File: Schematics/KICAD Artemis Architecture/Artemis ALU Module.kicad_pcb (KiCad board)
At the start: 4 copper layers, 66.2 x 46 mm, 11 parts, among them J1 B Input Socket, J2 A Input Socket, J3 F Output Socket, J4 Control Word Socket, J5 Flag Socket, J6 Power Socket, U1 74LS181, U2 74LS181, U3 74LS30

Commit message: Register PCB Created and Finished
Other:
- board text added: "ALU V1"
- board text removed: "ALU Module"

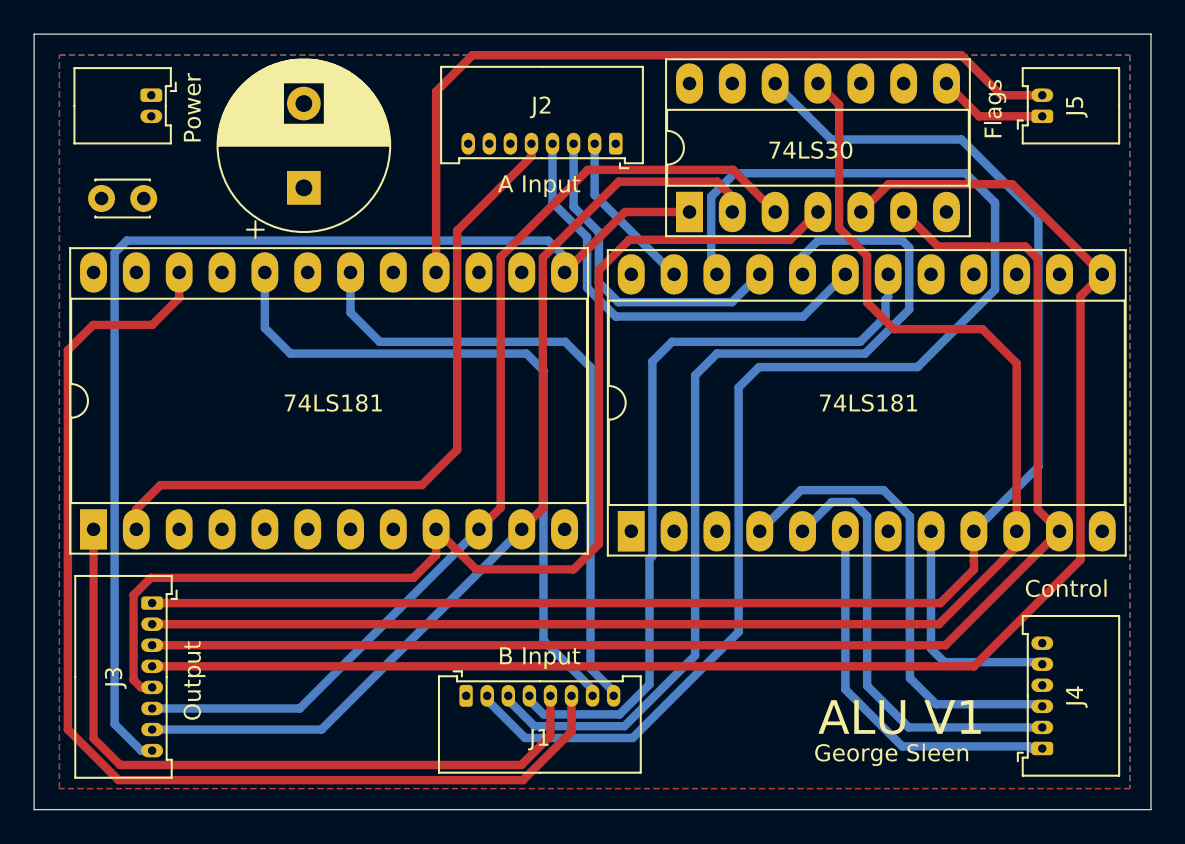
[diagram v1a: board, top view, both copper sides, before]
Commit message: Cleaned up ALU PCB
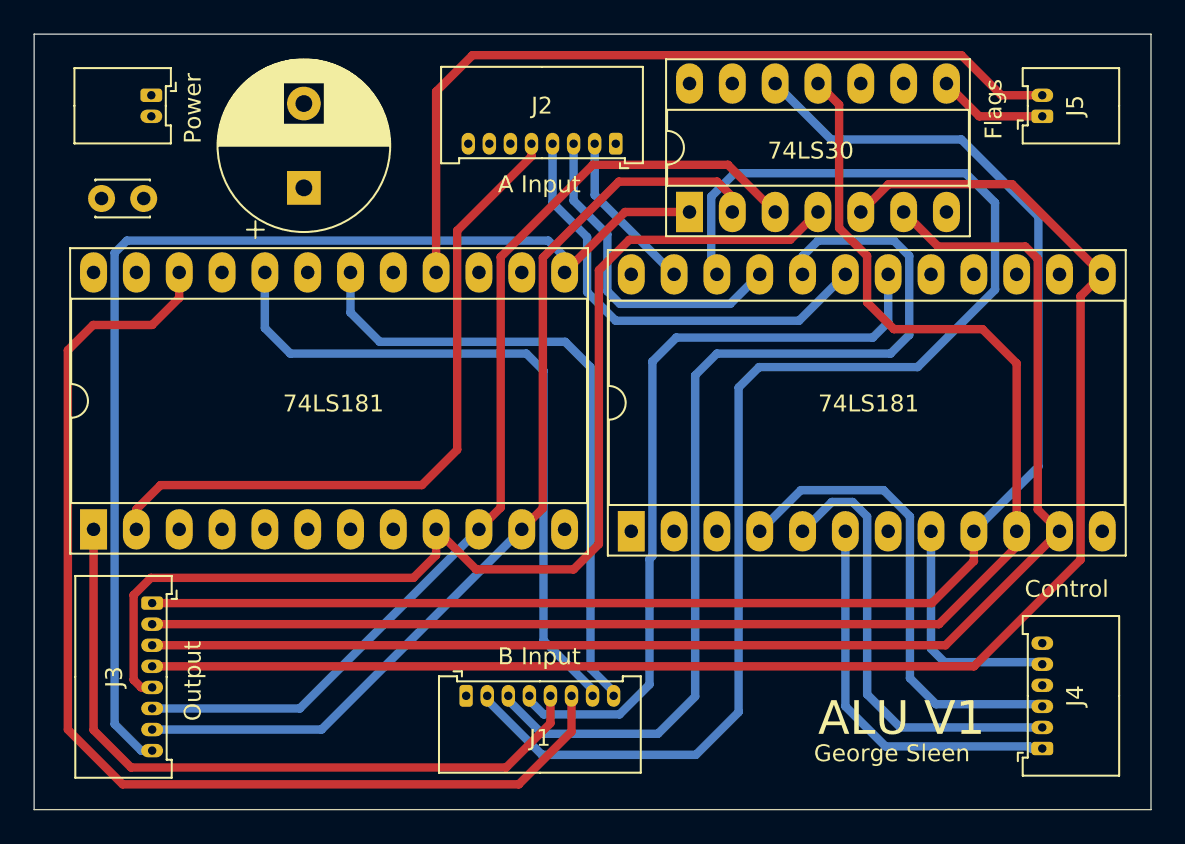
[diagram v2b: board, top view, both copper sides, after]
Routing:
- net /B1: track 78.9 -> 82.5 mm
- net /B2: track 56.3 -> 58.7 mm
- net /B4: track 43.2 -> 42.6 mm
- net /S0: track 63.9 -> 64.5 mm
- removed copper zone on B.Cu, net (none)
- removed copper zone on F.Cu, net (none)
